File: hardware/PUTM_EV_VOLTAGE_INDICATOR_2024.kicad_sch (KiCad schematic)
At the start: 10 parts, among them J1 WIRE, J2 WIRE, J3 SCREW_TERMINAL, J4 SCREW_TERMINAL, J5 SCREW_TERMINAL, J6 SCREW_TERMINAL, J7 WIRE, J8 WIRE

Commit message: schematic updated
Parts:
- added J10, J13, J14, J18, J19, J9: WIRE, symbol Connector:Conn_01x01_Pin
- added J11, J12: SCREW_TERMINAL, symbol Connector:Conn_01x01_Socket
- added J15, J16, J17, J20: PCB_PAD, symbol Connector:Conn_01x01_Socket
- added R2: 67k, symbol Device:R_Small
- added R3: 1k, symbol Device:R_Small
- added RD1: CDMM20M0F2500, CDMM:CDMM, symbol CDMM:CDMM2M50D4000DET
- added U1: LM321, Package_TO_SOT_SMD:SOT-23-5, symbol Amplifier_Operational:LM321
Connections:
- net at R1.1: now also J15.1 (Pin_1), R2.1, U1.5 (V+); no longer J1.1 (Pin_1)
- net at J7.1 (Pin_1): now also J10.1 (Pin_1)
- net at R1.2: now also J17.1 (Pin_1); no longer D1.2 (A)
- net at J2.1 (Pin_1): now also J14.1 (Pin_1); no longer D1.1 (K)
- net at J8.1 (Pin_1): now also J9.1 (Pin_1)
- new net: RD1.3, U1.1 (+)
- new net: J16.1 (Pin_1), R3.2, U1.2 (V-)
- new net: R2.2, R3.1, U1.3 (-)
- new net: J20.1 (Pin_1), U1.4
- new net: J1.1 (Pin_1), J13.1 (Pin_1)
- new net: J11.1 (Pin_1), RD1.1
- new net: J12.1 (Pin_1), RD1.2
- new net: D1.1 (K), J19.1 (Pin_1)
- new net: D1.2 (A), J18.1 (Pin_1)
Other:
- note added: "250:1 V_{OUT(3)} = V_{IN(1)} / 250 60 / 250 = 0.24"
- moved on the sheet: D1, J1, J2, J3, J4, J5, J6, J7, J8, R1

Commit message: esf changes
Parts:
- added J21, J22: SCREW, symbol Connector:Conn_01x01_Pin
- added J23, J24: EYE_CONNECTOR, symbol Connector:Conn_01x01_Socket
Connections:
- net at J8.1 (Pin_1), J9.1 (Pin_1): now also J23.1 (Pin_1)
- net at J10.1 (Pin_1), J7.1 (Pin_1): now also J24.1 (Pin_1)
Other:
- note added: "1*"
- note added: "1. All PCB_PAD / WIRE connections are wire directly soldered to a PAD on PCB and secured with adhesive 2. All SCREW / EYE_CONNECTOR connections are eye_connectors mounted to screws with a nut"
- note added: "2*"
- moved on the sheet: D1, J1, J10, J11, J12, J13, J14, J15, J16, J17, J18, J19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

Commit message: pcb done
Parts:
- removed RD1: CDMM20M0F2500, CDMM:CDMM, symbol CDMM:CDMM2M50D4000DET
- added RD1: CDMM20M0F2500DET, footprints:CDMM20M0F2500DET, symbol cdmm2m50d4000det:CDMM2M50D4000DET
- D1: value RED -> C4SMA-RGY-CT24QBB2
- J11, J12: value SCREW_TERMINAL -> PCB_PAD; footprint (none) -> Connector_Wire:SolderWire-0.1sqmm_1x01_D0.4mm_OD1mm_Relief
- J15, J16, J17, J20: footprint (none) -> Connector_Wire:SolderWire-0.1sqmm_1x01_D0.4mm_OD1mm_Relief
- R1, R2, R3: footprint (none) -> Resistor_SMD:R_0603_1608Metric
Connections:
- net REF: now reaches U1.1 (+)
- net REF: now also R2.2, R3.1
- net GND: now reaches J16.1 (Pin_1), R3.2, U1.2 (V-)
- net GND: now also J12.1 (Pin_1), RD1.2
- net LED_SINK: now reaches J20.1 (Pin_1), U1.4
- net 15V+: now reaches J15.1 (Pin_1), R1.1, R2.1, U1.5 (V+)
- net LED_POW: now reaches J17.1 (Pin_1), R1.2
- net HV+: now reaches J11.1 (Pin_1)
- net HV+: now also RD1.1
- new net HV_MES: RD1.3, U1.3 (-)
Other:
- moved on the sheet: J10, J11, J12, J13, J14, J15, J16, J9, R1, R2, R3

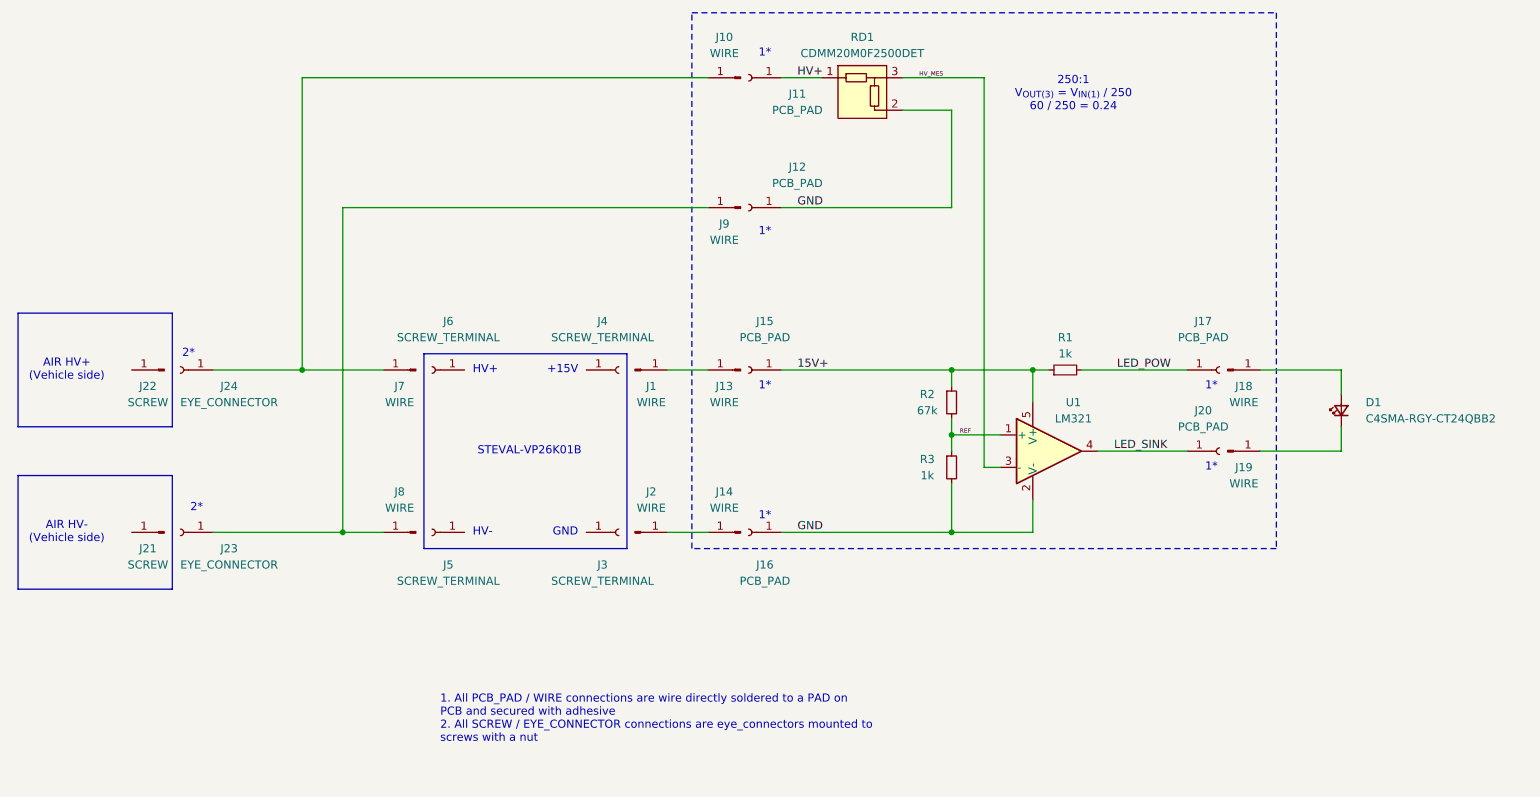
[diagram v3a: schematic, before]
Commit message: comparator fix
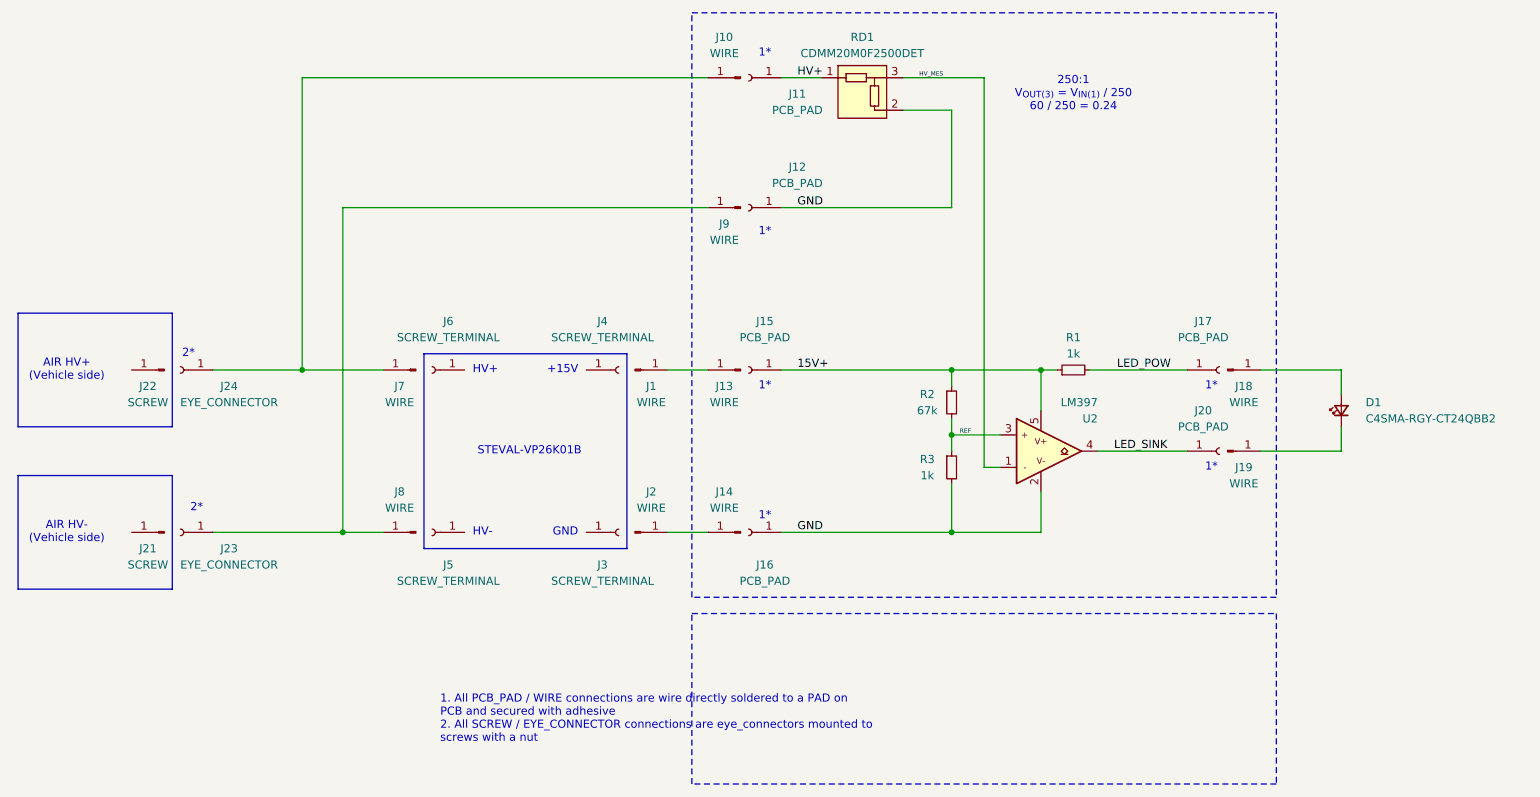
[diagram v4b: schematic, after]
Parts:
- removed U1: LM321, Package_TO_SOT_SMD:SOT-23-5, symbol Amplifier_Operational:LM321
- added U2: LM397, Package_TO_SOT_SMD:SOT-23-5, symbol Comparator:LM397
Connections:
- net 15V+: now also U2.5
- net GND: now also U2.2
- net HV_MES: now also U2.1
- net LED_SINK: now also U2.4
- net REF: now also U2.3
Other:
- moved on the sheet: R1
